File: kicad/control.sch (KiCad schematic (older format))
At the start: 24 parts, among them J301 DEBUG, J302 ROT_OUT, J303 DISPLAY, J304 ROT_IN, SW301 Encoder, U301 24LC1025, U302 STM32F030F4Px, Y301 MA-506-8MHz

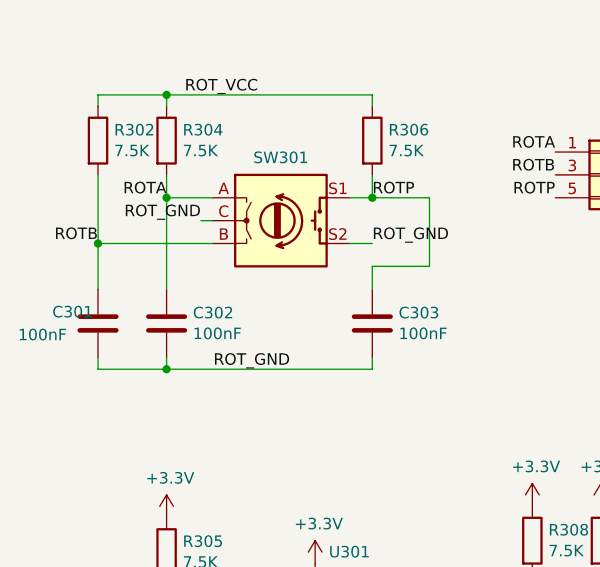
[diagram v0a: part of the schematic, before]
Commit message: Fixes in schematics (only) done during initial debug
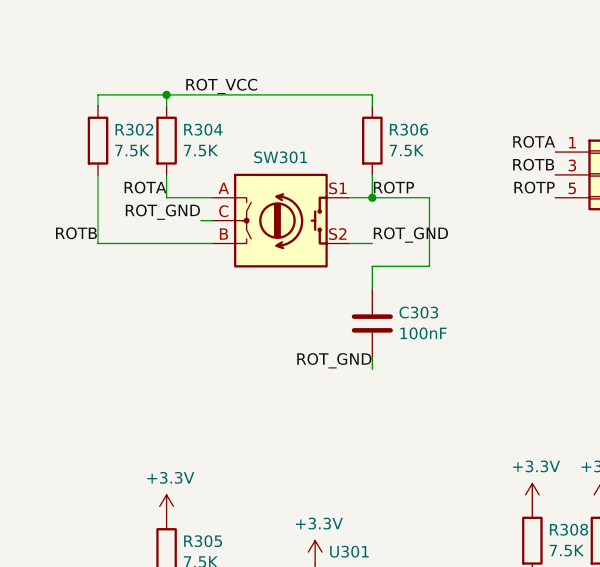
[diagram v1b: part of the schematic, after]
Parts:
- removed C301, C302: 100nF, Capacitors_SMD:C_0603_HandSoldering, symbol Device:C
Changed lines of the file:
@@
-$EndComp
-$Comp
-L Device:C C301
-U 1 1 60CEC57D
-P 1050 3550
-F 0 "C301" H 850 3600 50  0000 L CNN
-F 1 "100nF" H 700 3500 50  0000 L CNN
-F 2 "Capacitors_SMD:C_0603_HandSoldering" H 1088 3400 50  0001 C CNN
-F 3 "~" H 1050 3550 50  0001 C CNN
-	1    1050 3550
-	1    0    0    -1
-$EndComp
-$Comp
-L Device:C C302
-U 1 1 60CED103
-P 1350 3550
-F 0 "C302" H 1465 3596 50  0000 L CNN
-F 1 "100nF" H 1465 3505 50  0000 L CNN
-F 2 "Capacitors_SMD:C_0603_HandSoldering" H 1388 3400 50  0001 C CNN
-F 3 "~" H 1350 3550 50  0001 C CNN
-	1    1350 3550
-	1    0    0    -1
 $EndComp
 $Comp
@@
 $EndComp
 Wire Wire Line
-	1050 3400 1050 3200
-Connection ~ 1050 3200
-Wire Wire Line
-	1350 3400 1350 3000
-Connection ~ 1350 3000
-Wire Wire Line
 	2250 3400 2250 3300
 Wire Wire Line
@@
 Connection ~ 2250 3000
 Wire Wire Line
-	1050 3700 1050 3750
-Wire Wire Line
-	1050 3750 1350 3750
-Wire Wire Line
 	2250 3750 2250 3700
-Wire Wire Line
-	1350 3700 1350 3750
-Connection ~ 1350 3750
-Wire Wire Line
-	1350 3750 2250 3750
 NoConn ~ 10150 2200
 $Comp
@@
 NoConn ~ 3550 2900
 NoConn ~ 3800 3660
-Text Label 1890 3750 2    50   ~ 0
+Text Label 2250 3750 2    50   ~ 0
 ROT_GND
 $EndSCHEMATC
